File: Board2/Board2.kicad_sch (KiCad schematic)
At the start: 18 parts, among them J1 LEDs, J2 IR Therm, U1 MLX90614ESF-BCC-000-TU

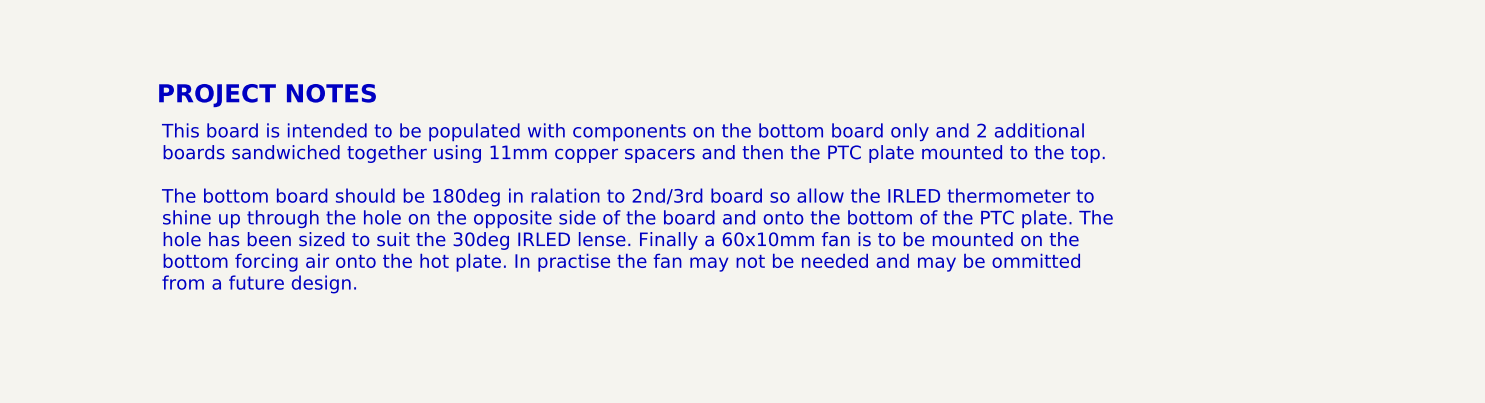
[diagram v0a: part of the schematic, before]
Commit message: Resolve library and ERC issues
No changes to design.
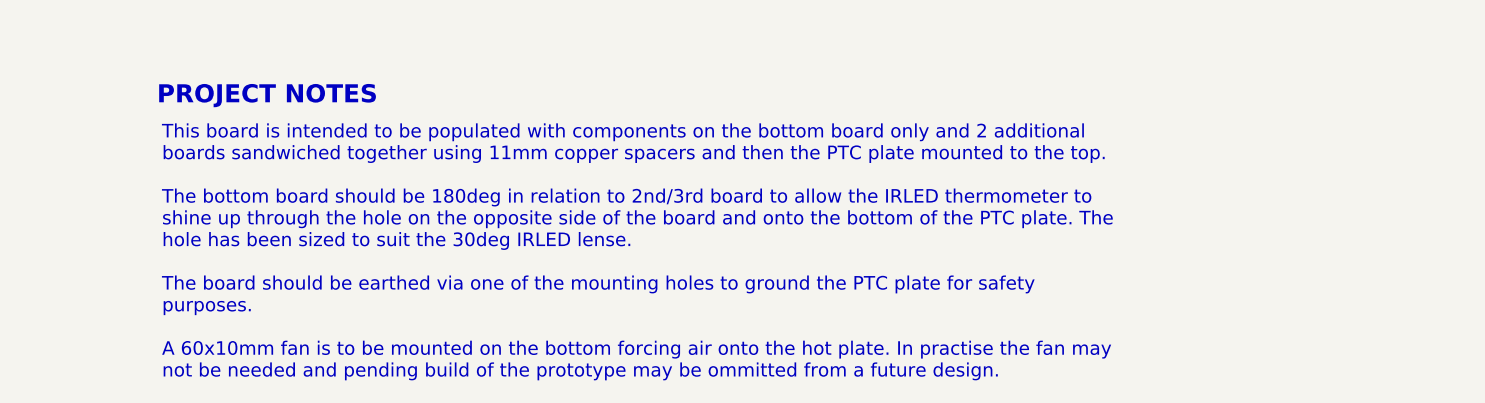
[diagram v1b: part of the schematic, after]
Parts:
- U1: footprint Colins Library:MLX90614xCC_MEL -> 0_Project:IRTHERMO_MLX90614xCC_MEL

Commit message: v1.2 release of board with bug fixes etc
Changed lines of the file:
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@@
 (kicad_sch
-	(version 20231120)
+	(version 20250114)
 	(generator "eeschema")
-	(generator_version "8.0")
+	(generator_version "9.0")
 	(paper "A4")
 	(title_block
@@
 		(company "Wattle Labs")
 	)
+	(text "Fan mounts"
+		(exclude_from_sim no)
+		(at 266.446 81.534 0)
+		(effects
+			(font
+				(size 1.27 1.27)
+				(thickness 0.1588)
+			)
+		)
+	)
+	(text "LEDs"
+		(exclude_from_sim no)
+		(at 116.078 31.242 0)
+		(effects
+			(font
+				(size 1.27 1.27)
+				(thickness 0.1588)
+			)
+		)
+	)
+	(text "PROJECT NOTES"
+		(exclude_from_sim no)
+		(at 159.385 128.905 0)
+		(effects
+			(font
+				(size 2 2)
+				(bold yes)
+				(color 53 60 207 1)
+			)
+			(justify left bottom)
+		)
+	)
+	(text "Board mounts"
+		(exclude_from_sim no)
+		(at 183.896 33.02 0)
+		(effects
+			(font
+				(size 1.27 1.27)
+				(thickness 0.1588)
+			)
+		)
+	)
+	(text "Infrared Thermometer LED"
+		(exclude_from_sim no)
+		(at 38.1 31.75 0)
+		(effects
+			(font
+				(size 1.27 1.27)
+				(thickness 0.1588)
+			)
+			(justify left top)
+		)
+	)
+	(text_box "This board is intended to be populated with components on the bottom board only and 2 additional boards sandwiched together using 11mm copper spacers and then the PTC plate mounted to the top.\n\nThe bottom board should be 180deg in relation to 2nd/3rd board to allow the IRLED thermometer to shine up through the hole on the opposite side of the board and onto the bottom of the PTC plate. The hole has been sized to suit the 30deg IRLED lens.\n\nThe board should be earthed via one of the mounting holes to ground the PTC plate for safety purposes.\n\nA 60x10mm fan is to be mounted on the bottom forcing air onto the hot plate. In practise the fan may not be needed.\n"
+		(exclude_from_sim no)
+		(at 158.75 129.54 0)
+		(size 124.46 48.26)
+		(margins 1.1249 1.1249 1.1249 1.1249)
+		(stroke
+			(width -0.0001)
+			(type solid)
+		)
+		(fill
+			(type none)
+		)
+		(effects
+			(font
+				(size 1.5 1.5)
+				(color 72 72 72 1)
+			)
+			(justify left top)
+		)
+	)
+	(text_box "DESIGN NOTES:\n\nThe main mounting holes are all earthed. 3 identical plates are intended to be connected to one another using 11mm copper standoffs that are offset and then connected to the mains earth connection. This is to earth the PTC heating element."
+		(exclude_from_sim no)
+		(at 231.14 31.75 0)
+		(size 50.038 20.066)
+		(margins 1.2025 1.2025 1.2025 1.2025)
+		(stroke
+			(width 0.5)
+			(type solid)
+			(color 250 236 0 1)
+		)
+		(fill
+			(type none)
+		)
+		(effects
+			(font
+				(size 1.27 1.27)
+				(color 0 0 0 1)
+			)
+			(justify left top)
+		)
+	)
+	(text_box "DESIGN NOTE:\n\n1. Current limiting resistors are located on the mainboard.\n2. Warning LED is intended to be red.\n3. Safe LED is intended to be green."
+		(exclude_from_sim no)
+		(at 114.808 56.642 0)
+		(size 44.45 15.24)
+		(margins 1.2025 1.2025 1.2025 1.2025)
+		(stroke
+			(width 0.5)
+			(type solid)
+			(color 200 200 200 1)
+		)
+		(fill
+			(type none)
+		)
+		(effects
+			(font
+				(size 1.27 1.27)
+				(color 0 0 0 1)
+			)
+			(justify left top)
+		)
+	)
+	(text_box "[${#}] ${TITLE}"
+		(exclude_from_sim no)
+		(at 11.938 11.938 0)
+		(size 273.05 13.335)
+		(margins 2.2499 2.2499 2.2499 2.2499)
+		(stroke
+			(width -0.0001)
+			(type default)
+		)
+		(fill
+			(type none)
+		)
+		(effects
+			(font
+				(size 3 3)
+				(thickness 0.375)
+			)
+		)
+	)
 	(junction
 		(at 182.118 64.262)
@@
 			"fIGPcw65zvkK8/XZ7DXnL6bP9PqARipmH1z7nm5O70+6lGlVR5Kf5EC4XQyxS3dwfmGXf9DkrJL8"
 			"Kx4/2RhWRcDc4fFbZAD1qdst1zkn3PvQzWbjwRasn/1zbg4J/b7v/gN/5ziO11/+y375//jYV+Xc"
-			"Kf8fETPUL2VTUKsAAAAASUVORK5CYII="
-		)
-	)
-	(text_box "This board is intended to be populated with components on the bottom board only and 2 additional boards sandwiched together using 11mm copper spacers and then the PTC plate mounted to the top.\n\nThe bottom board should be 180deg in relation to 2nd/3rd board to allow the IRLED thermometer to shine up through the hole on the opposite side of the board and onto the bottom of the PTC plate. The hole has been sized to suit the 30deg IRLED lense.\n\nThe board should be earthed via one of the mounting holes to ground the PTC plate for safety purposes.\n\nA 60x10mm fan is to be mounted on the bottom forcing air onto the hot plate. In practise the fan may not be needed and pending build of the prototype may be ommitted from a future design.\n"
-		(exclude_from_sim no)
-		(at 158.75 129.54 0)
-		(size 124.46 48.26)
-		(stroke
-			(width -0.0001)
-			(type default)
-		)
-		(fill
-			(type none)
-		)
-		(effects
-			(font
-				(size 1.5 1.5)
-				(color 72 72 72 1)
-			)
-			(justify left top)
-		)
-	)
-	(text_box "DESIGN NOTES:\n\nThe main mounting holes are all earthed. 3 identical plates are intended to be connected to one another using 11mm copper standoffs that are offset and then connected to the mains earth connection. This is to earth the PTC heating element."
-		(exclude_from_sim no)
-		(at 231.14 31.75 0)
-		(size 50.038 20.066)
-		(stroke
-			(width 0.5)
-			(type solid)
-			(color 250 236 0 1)
-		)
-		(fill
-			(type none)
-		)
-		(effects
-			(font
-				(size 1.27 1.27)
-				(color 0 0 0 1)
-			)
-			(justify left top)
-		)
-	)
-	(text_box "DESIGN NOTE:\n\n1. Current limiting resistors are located on the mainboard.\n2. Warning LED is intended to be red.\n3. Safe LED is intended to be green."
-		(exclude_from_sim no)
-		(at 114.808 56.642 0)
-		(size 44.45 15.24)
-		(stroke
-			(width 0.5)
-			(type solid)
-			(color 200 200 200 1)
-		)
-		(fill
-			(type none)
-		)
-		(effects
-			(font
-				(size 1.27 1.27)
-				(color 0 0 0 1)
-			)
-			(justify left top)
-		)
-	)
-	(text_box "[${#}] ${TITLE}"
-		(exclude_from_sim no)
-		(at 11.938 11.938 0)
-		(size 273.05 13.335)
-		(stroke
-			(width -0.0001)
-			(type default)
-		)
-		(fill
-			(type none)
-		)
-		(effects
-			(font
-				(size 3 3)
-				(thickness 0.375)
-			)
-		)
-	)
-	(text "Fan mounts"
-		(exclude_from_sim no)
-		(at 266.446 81.534 0)
-		(effects
-			(font
-				(size 1.27 1.27)
-				(thickness 0.1588)
-			)
-		)
-	)
-	(text "LEDs"
-		(exclude_from_sim no)
-		(at 116.078 31.242 0)
-		(effects
-			(font
-				(size 1.27 1.27)
-				(thickness 0.1588)
-			)
-		)
-	)
-	(text "PROJECT NOTES"
-		(exclude_from_sim no)
-		(at 159.385 128.905 0)
-		(effects
-			(font
-				(size 2 2)
-				(bold yes)
-				(color 53 60 207 1)
-			)
-			(justify left bottom)
-		)
-	)
-	(text "Board mounts"
-		(exclude_from_sim no)
-		(at 183.896 33.02 0)
-		(effects
-			(font
-				(size 1.27 1.27)
-				(thickness 0.1588)
-			)
-		)
-	)
-	(text "Infrared Thermometer LED"
-		(exclude_from_sim no)
-		(at 38.1 31.75 0)
-		(effects
-			(font
-				(size 1.27 1.27)
-				(thickness 0.1588)
-			)
-			(justify left top)
+			"Kf8fETPUL2VTUKsAAAAASUVORK5CYIIAAAAAAAAAAAAAAAAAAAAAAAAAAAAAAAAAAAAAAAAAEPVb"
+			"YIJ/AAA49Flggn8AAAAAAAABAAAAAAAAAAAAAADAi2cAAGAAAAIAAAABAAAAsL9kYIJ/AADAi2cA"
+			"AGAAAAAAAAAAAAAAyL9kYIJ/AAAAAAAAAAAAAMCLZwAAYAAAAAAAAAAAAAAAAAAAAAAAAAAAAAAA"
+			"AAAAAAAAAAAAAAAAAAAAAAAAAAAAAAAAAAAAAAAAAAAAAAAAAAAAAAAAAAAAAAAAAAAAAAAAAAAA"
+			"AAAAAAAAAAAAAAAAAAAAAAAAAAAAAAAAAAAAAAAABgAAAAYAAAAGAAAABgAAAAAAAAAAAAAAAAAA"
+			"AAAAAAAAAAAAAAAAAAAAAAAAAAAAAAAAAAAAAAAAAAAAAAAAAAAAAAAAAAAAAAAAAAAAAAAAAAAA"
+			"AAAAAAAAAAAAAAAAAAAAAAAAAAAAAAAAAAAAAAAAAAAAAAAAAAAAAAAAAAAAAAAAAAAAAAAAAAAA"
+			"AAAAAAAAAAAAAAAAAAAAAAAAAAYAAAAGAAAABgAAAAYAAAAAAAAAAAAAAAAAAAAAAAAAAAAAAAAA"
+			"AAAAAAAAAAAAAAAAAAAAAAAAAAAAAAAAAAAAAAAAAAAAAAAAAAAAAAAAAAAAAAAAAAAAAAAAAAAA"
+			"AAAAAAAAAAAAAAAAAAAAAAAAAAAAAAAAAAAAAAAAAAAAAAAAAAAAAAAAAAAAAAAAAAAAAAAAAAAA"
+			"AAAAAAAAAAAGAAAABgAAAAYAAAAGAAAAAAAAAAAAAAAAAAAAAAAAAAAAAAAAAAAAAAAAAAAAAAAA"
+			"AAAAyPZbYIJ/AAAAAQIDAAAAAADsMYCCfwAAwItnAABgAABxAAAAAgAAAAIAAAACAAAAAAAAAAAA"
+			"AAAAAAAAAAAAAAAAAAAAAAAAAAAAAAAAAAAAAAAAAAAAAAAAAAAAAAAAAAAAAAAAAAAAAAAAAAAA"
+			"AAAAAAAAAAAAAAAAAAAAAAAAAAAAAAAAAAAAAAAGAAAABgAAAAYAAAAGAAAAAAAAAAAAAAAAAAAA"
+			"AAAAAAAAAAAAAAAAAAAAAAAAAAAAAAAAcQAAAHEAAABxAAAAcQAAAAAAAAAAAAAAAAAAAAAAAAAA"
+			"AAAAAAAAAAAAAAAAAAAAAAAAAAAAAAAAAAAAAAAAAAAAAAAAAAAAAAAAAAAAAAAAAAAAAAAAAAAA"
+			"AAAAAAAAAAAAAAAAAAAAAAAABgAAAAYAAAAGAAAABgAAAAAAAAAAAAAAAAAAAAAAAAAAAAAAAAAA"
+			"AAAAAAAAAAAAAAAAAAEAAAABAAAAAQAAAAEAAAAAAAAAAAAAAAAAAAAAAAAAAAAAAAAAAAAAAAAA"
+			"AAAAAAAAAAAAAAAAAAAAAAAAAAAAAAwePWLxGH9ohlOGtVVLP53jdbwKk1N1IU0401d/zPfpsum3"
+			"rqFm9z3rTtO0/R9PsNJ0mwt7LSrKFLa1srSJYoraJFCpHGigBVVQAFAAAAArCUnNuUndsYajqOn6"
+			"Rp99q2rX1vZaXZQvcXN5dyrFFbxIpZ5JHYgKqqCSxIAAJNEYuTUYq7YHgsvxP8f/ABGcwfAbw5pj"
+			"+HFlWOT4g+MRcxabKpaMmTTLSMLLqcZjLFZhLb2z7kMU8w3hOiNOnDWs+j0W99bXvotbX3dmK76H"
+			"MeKfB/hLw9pcOsftTftAtqFje3TxRWGp6rF4R0BmkZmNolnDKhvImjCoYL6e83KjdncNUar2oQtt"
+			"5u6Xe2l3rb/ITXcu+H/iPDp2i2XhP9nf9nXX5vD9rsW1a60lPBGh2DSzMz7ku0iudgBeUva2U6ks"
+			"OSzHAqSlK9epbf8AvPRabd3pv+QX7I6lvC/x68WlJfEnxL0rwNpzEv8A2V4A06PUb2BhlQjapqMb"
+			"wzRMPnIXToXDbVDkKTJlzU4rSN35/wCS/wAx69SPSv2Zvg3avZXviXwxJ44122iijj1r4jXs/ie6"
+			"iZM/PC168q2xZmZmW3WJCSPlwFAueLqSk5Q91XbtHRK/b9NRcqPcbGxstMtLfT9Ns4LSwgUJFbW0"
+			"axxxKOgVQAAPYVhKTm+aTuyi1UgeP63/AMl++GfX/kT/ABN/6W6DXLP/AHqH+GX5wPfw3/IhxX/X"
+			"6h/6RiT2Cuo8A5Lxf4A8CfEKxg0zx94K0HxLpsLmSO01/TYL+KNyMFlSVWAOOMgVcKk6d1CTV+wr"
+			"Jnl6/sxfBaymuZvDHhrUfCCXIQTW3w/8Q6p4Wt5igIUvBp1xBGzAE8lSeTWjxNSUFCTulfdJ7767"
+			"hyrcYvwp+IfhK3+1eAfjb4s1D7BI01l4V8bS2N/p90m8sbWe+Nm2ohSpKJcNcTSRnY7LcBDFISqx"
+			"m7yilpbTTpa+9r9+4WsegaBr3hj4reFdasNQ0UtA5m0bxB4V1+CN5rGYxjzrK8hyyNmOVGBBeKWK"
+			"WOWNpIpY5GyacHox7nyR+zz4B8L6n4Y1fwv4P+JWr+C/iv4G1O78P+I7TwTNDZW7/Z7ia3hu38P3"
+			"SXGn2gv4reK88yG2RmZ32S4MgPbiZyTTlG8Wla+r77qz3vv0fzJij3mfxX8aPh2FuvH3hrTvHPhY"
+			"uvn638PNPuLS/wBOVjgtJo0s1w9xEgVmaS2uJJ2LqqWjYLnmUadT4XZ+f+eg9T1zwp4u8L+O/D+m"
+			"+K/BniCw1vw1qCs1tqemTrPDMFYowDqSMqysrDqrKQQCCKznCUG4yVmO9zoqkD561f4Laj4T1XxF"
+			"42+AOs23hbxTrN9Lq+seHL9Gn0HxRQ=="
 		)
 	)
@@
 		)
 	)
+	(embedded_fonts no)
 )
